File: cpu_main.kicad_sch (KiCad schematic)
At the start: 10 parts, among them Q1 9018G, U1 Z80CPU, U2 74LS244, U3 74LS257, U4 74LS00, U5 27128, U6 74LS257, U7 27128, U8 74LS273, U9 2764

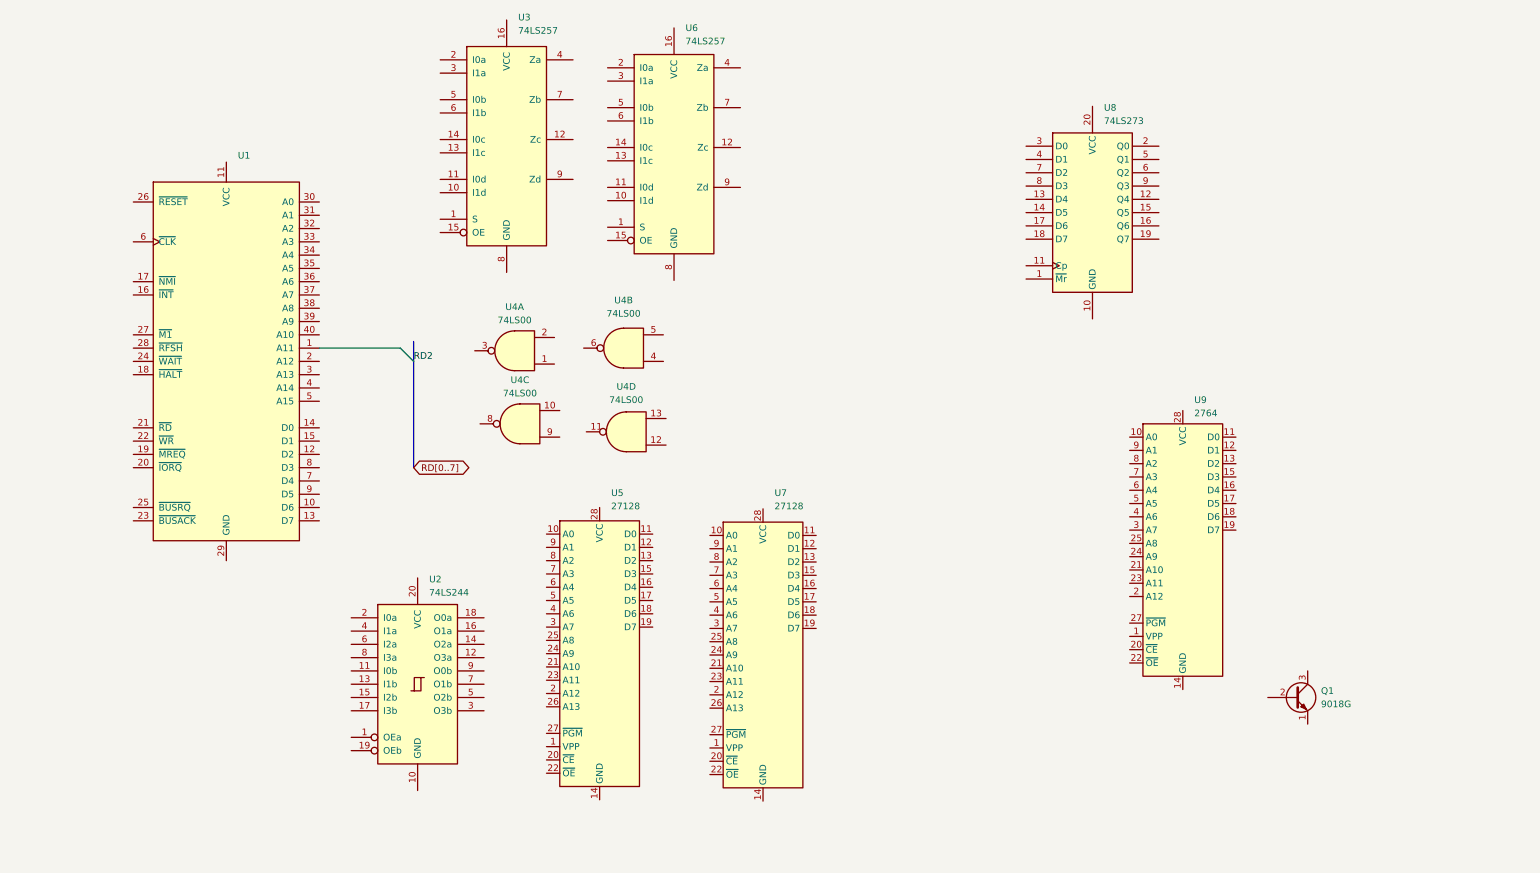
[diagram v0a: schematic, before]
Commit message: Started video_cassette sch
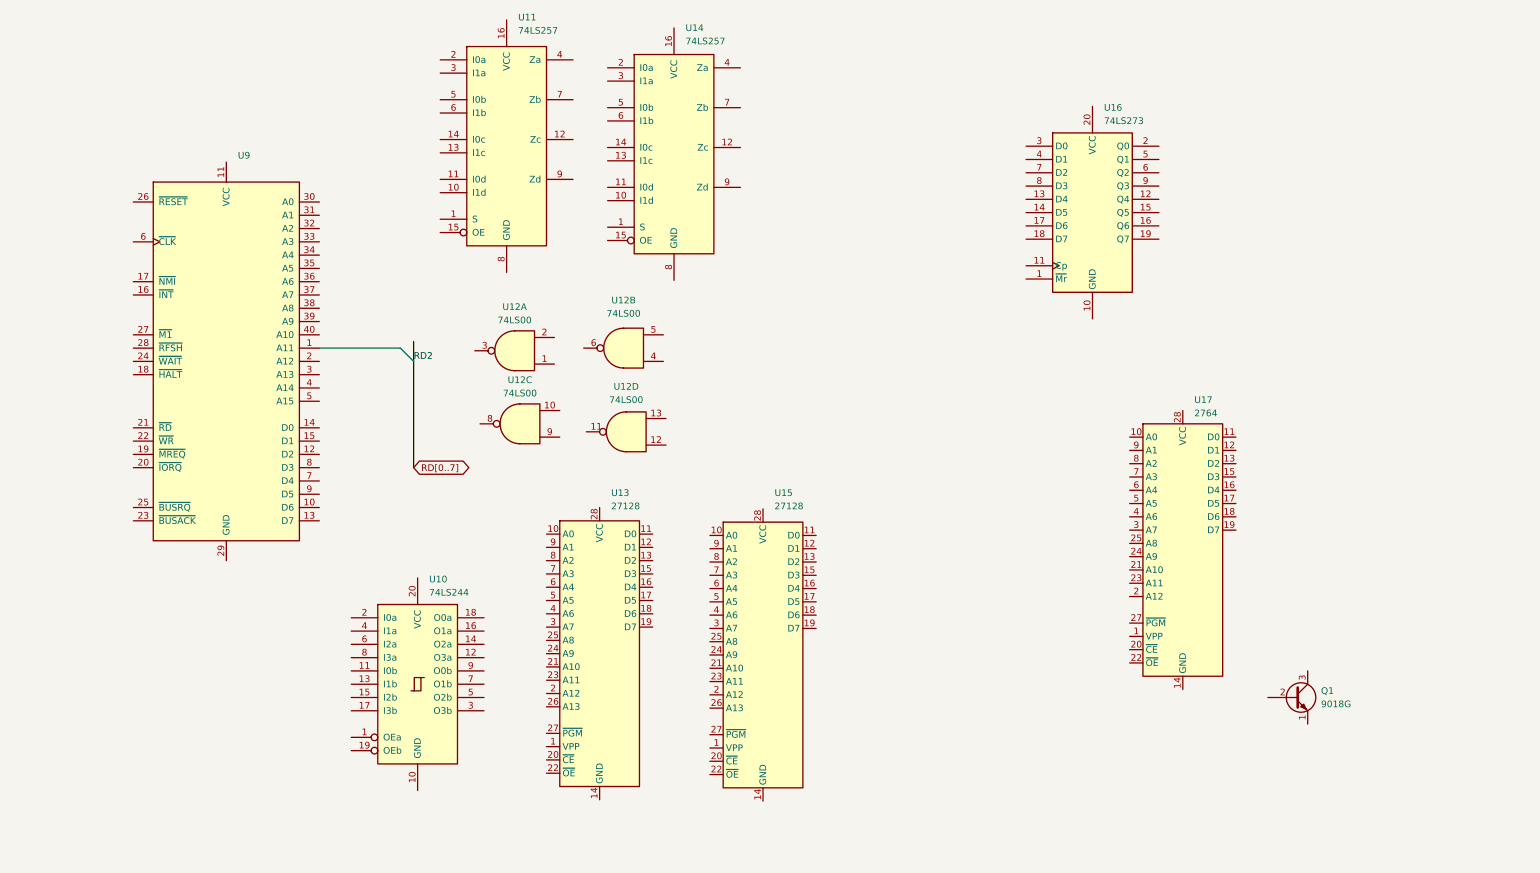
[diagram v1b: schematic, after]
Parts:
- Q1: footprint (none) -> Package_TO_SOT_THT:TO-92
- renumbered U2 to U10, U3 to U11, U4 to U12, U5 to U13, U6 to U14, U7 to U15, U8 to U16, U9 to U17, U1 to U9
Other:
- title: (none) -> Main Circuit
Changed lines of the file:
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@@
 	(generator_version "8.0")
 	(paper "A4")
+	(title_block
+		(title "Main Circuit")
+	)
 	(bus_entry
 		(at 84.074 79.502)
@@
 		(dnp no)
 		(fields_autoplaced yes)
-		(property "Reference" "U2"
+		(property "Reference" "U10"
 			(at 89.5701 123.698 0)
 			(effects
@@
 			(project "Laser-500"
 				(path "/c1a6b1ae-77c2-4767-93cc-3749547878e9/f9690aae-74b6-4c7d-a01b-51dcb981f67f"
-					(reference "U2")
+					(reference "U10")
 					(unit 1)
 				)
@@
 		(dnp no)
 		(fields_autoplaced yes)
-		(property "Reference" "U4"
+		(property "Reference" "U12"
 			(at 126.7543 70.358 0)
 			(effects
@@
 			(project "Laser-500"
 				(path "/c1a6b1ae-77c2-4767-93cc-3749547878e9/f9690aae-74b6-4c7d-a01b-51dcb981f67f"
-					(reference "U4")
+					(reference "U12")
 					(unit 2)
 				)
@@
 		(dnp no)
 		(fields_autoplaced yes)
-		(property "Reference" "U4"
+		(property "Reference" "U12"
 			(at 127.2623 86.868 0)
 			(effects
@@
 			(project "Laser-500"
 				(path "/c1a6b1ae-77c2-4767-93cc-3749547878e9/f9690aae-74b6-4c7d-a01b-51dcb981f67f"
-					(reference "U4")
+					(reference "U12")
 					(unit 4)
 				)
@@
 		(dnp no)
 		(fields_autoplaced yes)
-		(property "Reference" "U6"
+		(property "Reference" "U14"
 			(at 138.5921 18.288 0)
 			(effects
@@
 			(project "Laser-500"
 				(path "/c1a6b1ae-77c2-4767-93cc-3749547878e9/f9690aae-74b6-4c7d-a01b-51dcb981f67f"
-					(reference "U6")
+					(reference "U14")
 					(unit 1)
 				)
@@
 			)
 		)
-		(property "Footprint" ""
+		(property "Footprint" "Package_TO_SOT_THT:TO-92"
 			(at 260.096 143.764 0)
 			(effects
@@
 		(dnp no)
 		(fields_autoplaced yes)
-		(property "Reference" "U5"
+		(property "Reference" "U13"
 			(at 124.3681 107.188 0)
 			(effects
@@
 			(project "Laser-500"
 				(path "/c1a6b1ae-77c2-4767-93cc-3749547878e9/f9690aae-74b6-4c7d-a01b-51dcb981f67f"
-					(reference "U5")
+					(reference "U13")
 					(unit 1)
 				)
@@
 		(dnp no)
 		(fields_autoplaced yes)
-		(property "Reference" "U7"
+		(property "Reference" "U15"
 			(at 155.6101 107.188 0)
 			(effects
@@
 			(project "Laser-500"
 				(path "/c1a6b1ae-77c2-4767-93cc-3749547878e9/f9690aae-74b6-4c7d-a01b-51dcb981f67f"
-					(reference "U7")
+					(reference "U15")
 					(unit 1)
 				)
@@
 		(dnp no)
 		(fields_autoplaced yes)
-		(property "Reference" "U1"
+		(property "Reference" "U9"
 			(at 52.9941 42.672 0)
 			(effects
@@
 			(project "Laser-500"
 				(path "/c1a6b1ae-77c2-4767-93cc-3749547878e9/f9690aae-74b6-4c7d-a01b-51dcb981f67f"
-					(reference "U1")
+					(reference "U9")
 					(unit 1)
 				)
@@
 		(dnp no)
 		(fields_autoplaced yes)
-		(property "Reference" "U4"
+		(property "Reference" "U12"
 			(at 106.9423 85.598 0)
 			(effects
@@
 			(project "Laser-500"
 				(path "/c1a6b1ae-77c2-4767-93cc-3749547878e9/f9690aae-74b6-4c7d-a01b-51dcb981f67f"
-					(reference "U4")
+					(reference "U12")
 					(unit 3)
 				)
@@
 		(dnp no)
 		(fields_autoplaced yes)
-		(property "Reference" "U9"
+		(property "Reference" "U17"
 			(at 235.8741 89.408 0)
 			(effects
@@
 			(project "Laser-500"
 				(path "/c1a6b1ae-77c2-4767-93cc-3749547878e9/f9690aae-74b6-4c7d-a01b-51dcb981f67f"
-					(reference "U9")
+					(reference "U17")
 					(unit 1)
 				)
@@
 		(dnp no)
 		(fields_autoplaced yes)
-		(property "Reference" "U4"
+		(property "Reference" "U12"
 			(at 105.9263 71.628 0)
 			(effects
@@
 			(project "Laser-500"
 				(path "/c1a6b1ae-77c2-4767-93cc-3749547878e9/f9690aae-74b6-4c7d-a01b-51dcb981f67f"
-					(reference "U4")
+					(reference "U12")
 					(unit 1)
 				)
@@
 		(dnp no)
 		(fields_autoplaced yes)
-		(property "Reference" "U8"
+		(property "Reference" "U16"
 			(at 218.6021 33.528 0)
 			(effects
@@
 			(project "Laser-500"
 				(path "/c1a6b1ae-77c2-4767-93cc-3749547878e9/f9690aae-74b6-4c7d-a01b-51dcb981f67f"
-					(reference "U8")
+					(reference "U16")
 					(unit 1)
 				)
@@
 		(dnp no)
 		(fields_autoplaced yes)
-		(property "Reference" "U3"
+		(property "Reference" "U11"
 			(at 106.5881 16.256 0)
 			(effects
@@
 			(project "Laser-500"
 				(path "/c1a6b1ae-77c2-4767-93cc-3749547878e9/f9690aae-74b6-4c7d-a01b-51dcb981f67f"
-					(reference "U3")
+					(reference "U11")
 					(unit 1)
 				)

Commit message: Updated symbols
74LS257
GA1
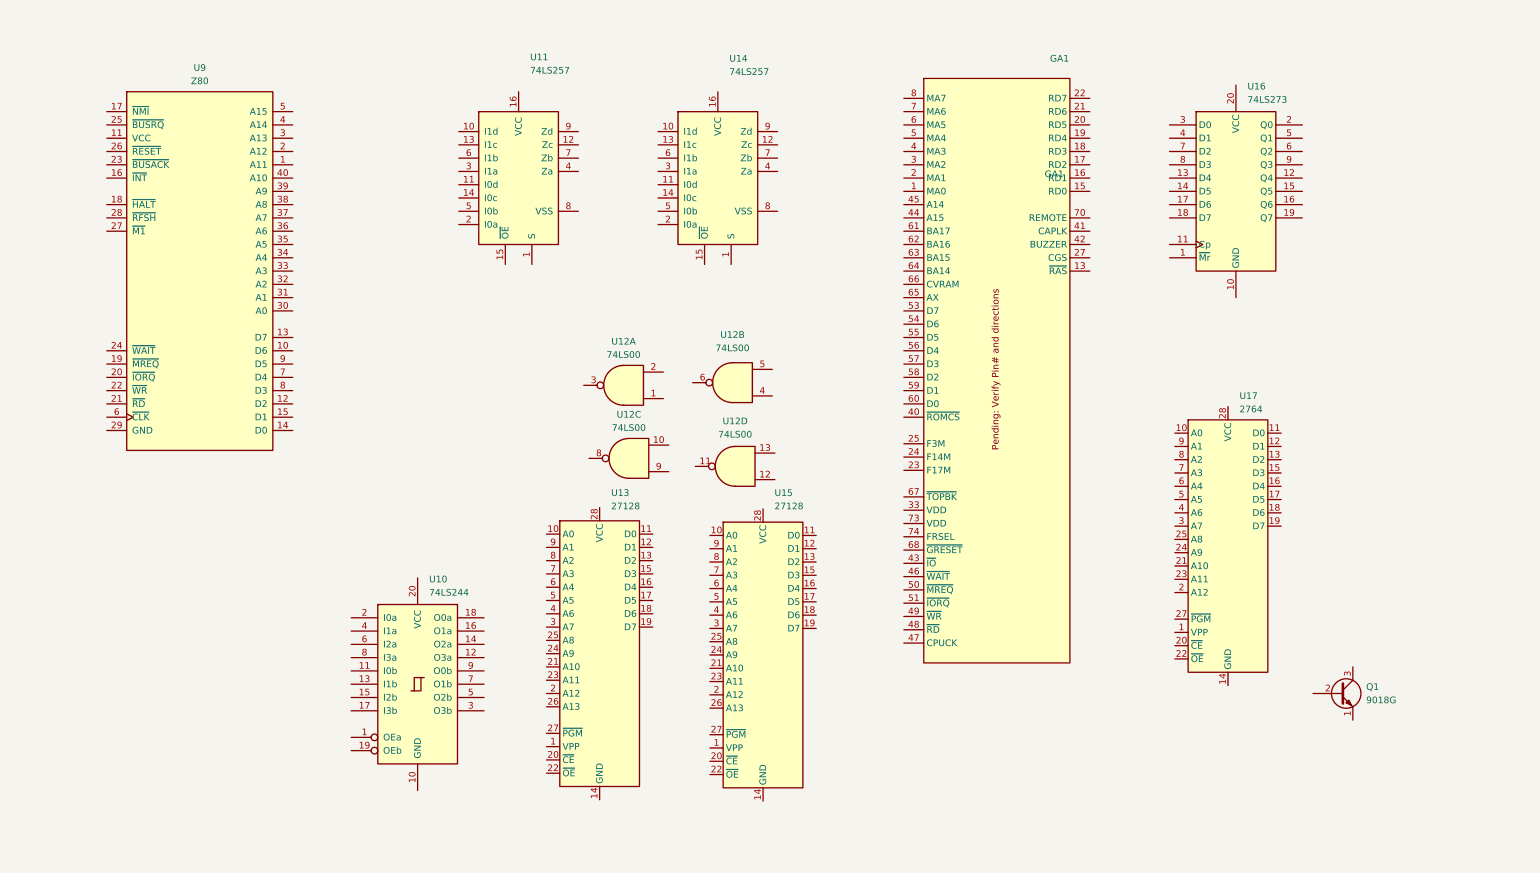
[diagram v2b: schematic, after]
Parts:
- removed U11, U14: 74LS257, Package_DIP:DIP-16_W7.62mm, symbol 74xx:74LS257
- removed U9: Z80CPU, Package_DIP:DIP-40_W15.24mm, symbol CPU:Z80CPU
- added GA1: GA1, symbol Laser500:GA1
- added U11, U14: 74LS257, symbol Laser500:74LS257
- added U9: Z80, symbol Laser500:Z80
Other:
- moved on the sheet: Q1, U12A, U12B, U12C, U12D, U16, U17

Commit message: More Laser 500 symbols
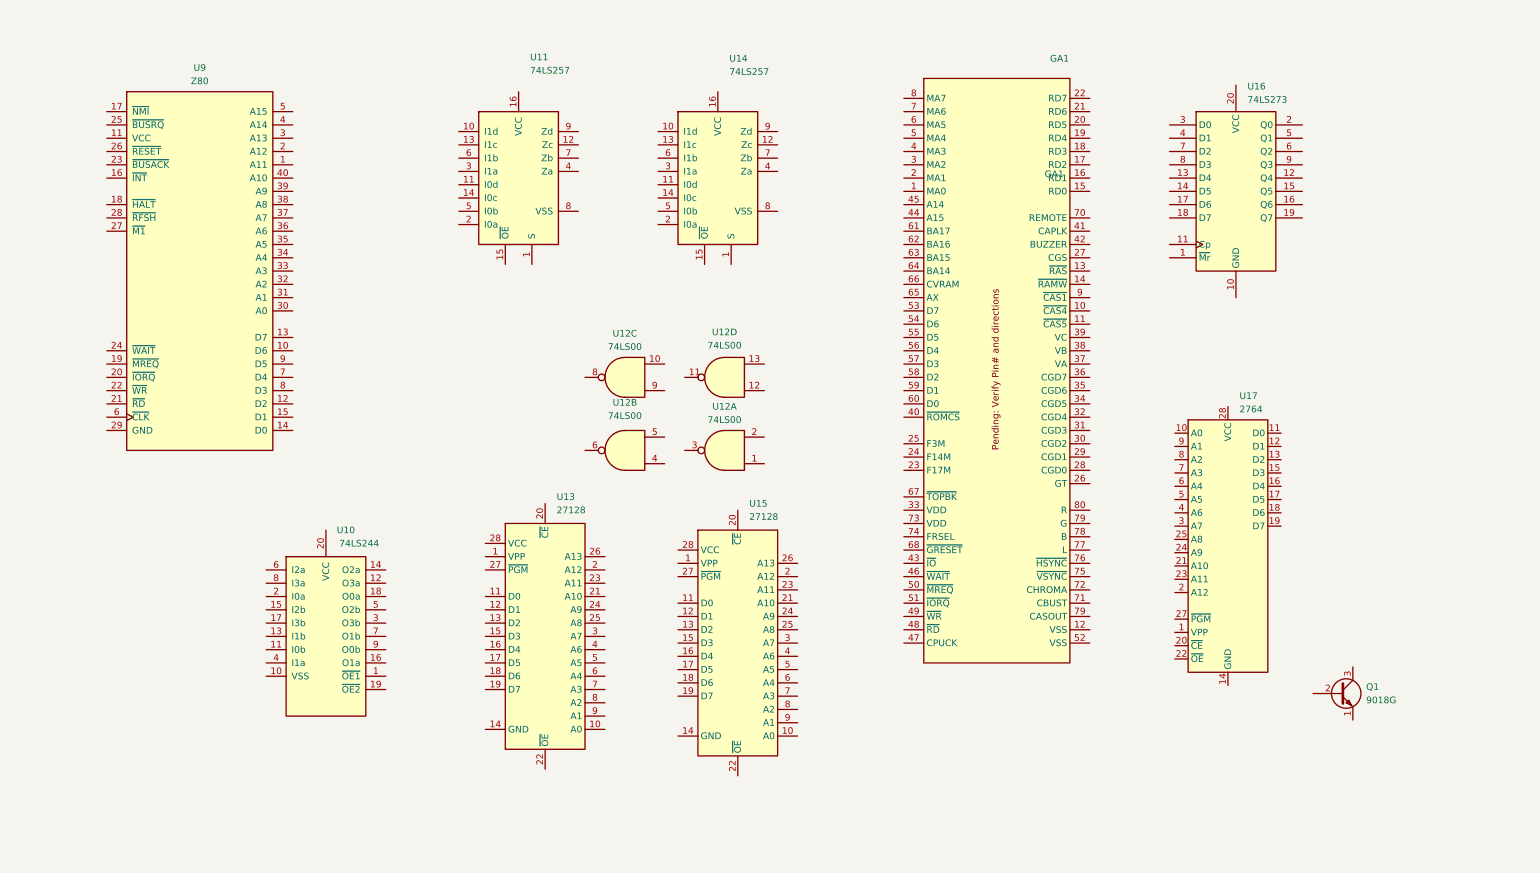
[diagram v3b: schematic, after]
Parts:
- removed U10: 74LS244, Package_DIP:DIP-20_W7.62mm, symbol 74xx:74LS244
- removed U13, U15: 27128, Package_DIP:DIP-28_W15.24mm, symbol Memory_EPROM:27128
- added U10: 74LS244, symbol Laser500:74LS244
- added U13, U15: 27128, Package_DIP:DIP-28_W15.24mm, symbol Laser500:27128
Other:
- moved on the sheet: U12A, U12B, U12C, U12D

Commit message: A few Boxing day updates
1. Add Laser 500 Mainboard PCB photo
2. Updated Main circuit ICs and their symbols.
3. Updated references according to PCB photo
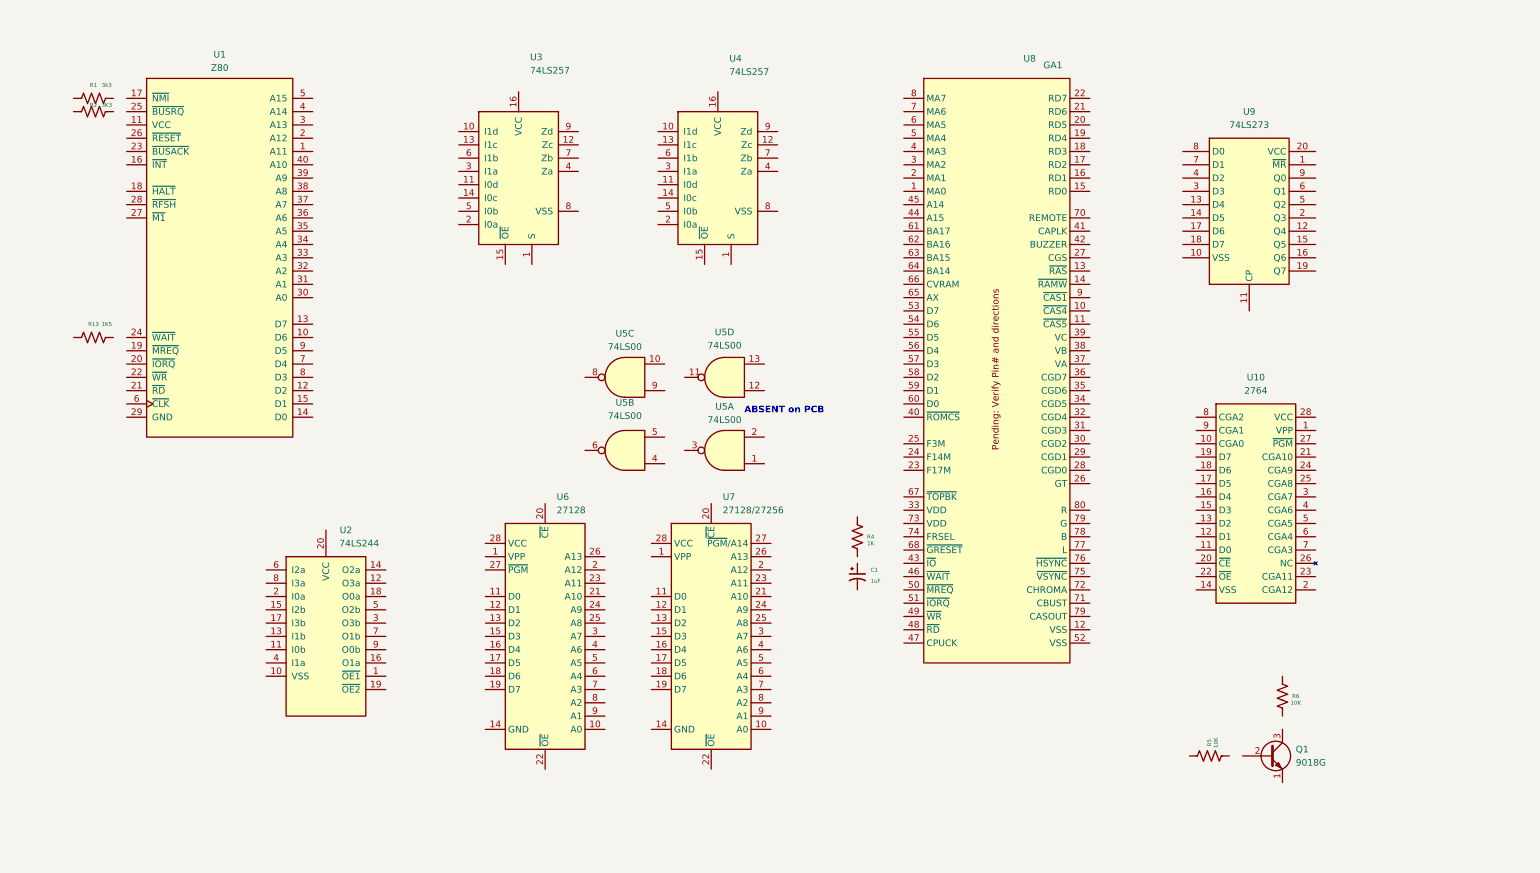
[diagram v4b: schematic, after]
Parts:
- removed U15: 27128, Package_DIP:DIP-28_W15.24mm, symbol Laser500:27128
- removed U16: 74LS273, Package_DIP:DIP-20_W7.62mm, symbol 74xx:74LS273
- removed U17: 2764, Package_DIP:DIP-28_W15.24mm, symbol Memory_EPROM:2764
- added C1: 1uF, symbol Device:C_Polarized_Small_US
- added R1: 3k3, Resistor_THT:R_Axial_DIN0207_L6.3mm_D2.5mm_P7.62mm_Horizontal, symbol Device:R_US
- added R13: 1K5, Resistor_THT:R_Axial_DIN0207_L6.3mm_D2.5mm_P7.62mm_Horizontal, symbol Device:R_US
- added R2: 3K3, Resistor_THT:R_Axial_DIN0207_L6.3mm_D2.5mm_P7.62mm_Horizontal, symbol Device:R_US
- added R4: 1K, Resistor_THT:R_Axial_DIN0207_L6.3mm_D2.5mm_P7.62mm_Horizontal, symbol Device:R_US
- added R5, R6: 10K, Resistor_THT:R_Axial_DIN0207_L6.3mm_D2.5mm_P7.62mm_Horizontal, symbol Device:R_US
- added U10: 2764, Package_DIP:DIP-28_W15.24mm, symbol Laser500:2764
- added U7: 27128/27256, Package_DIP:DIP-28_W15.24mm, symbol Laser500:27128/27256
- added U9: 74LS273, symbol Laser500:74LS273
- renumbered U9 to U1, U10 to U2, U11 to U3, U14 to U4, U12 to U5, U13 to U6, GA1 to U8
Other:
- note added: "ABSENT on PCB"
- moved on the sheet: Q1, U1
